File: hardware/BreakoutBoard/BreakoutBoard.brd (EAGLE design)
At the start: 90 x 56 mm, 67 parts, among them J1 CON-71741-2184-TOP, J2 CON-71741-2184-BOT, J3 CON-2X11-RASTER, J4 CON-2X10-RASTER, J5 CON-2X10-RASTER, J6 CON-2X11-RASTER, J7 CON-HTST-105-04-D-RA, M1 MOUNT-HOLE3.3, M2 MOUNT-HOLE3.3, M3 MOUNT-HOLE3.3, M4 MOUNT-HOLE3.3, M5 FIDUCIAL1X2, M6 FIDUCIAL1X2, M7 FIDUCIAL1X2, M8 FIDUCIAL1X2

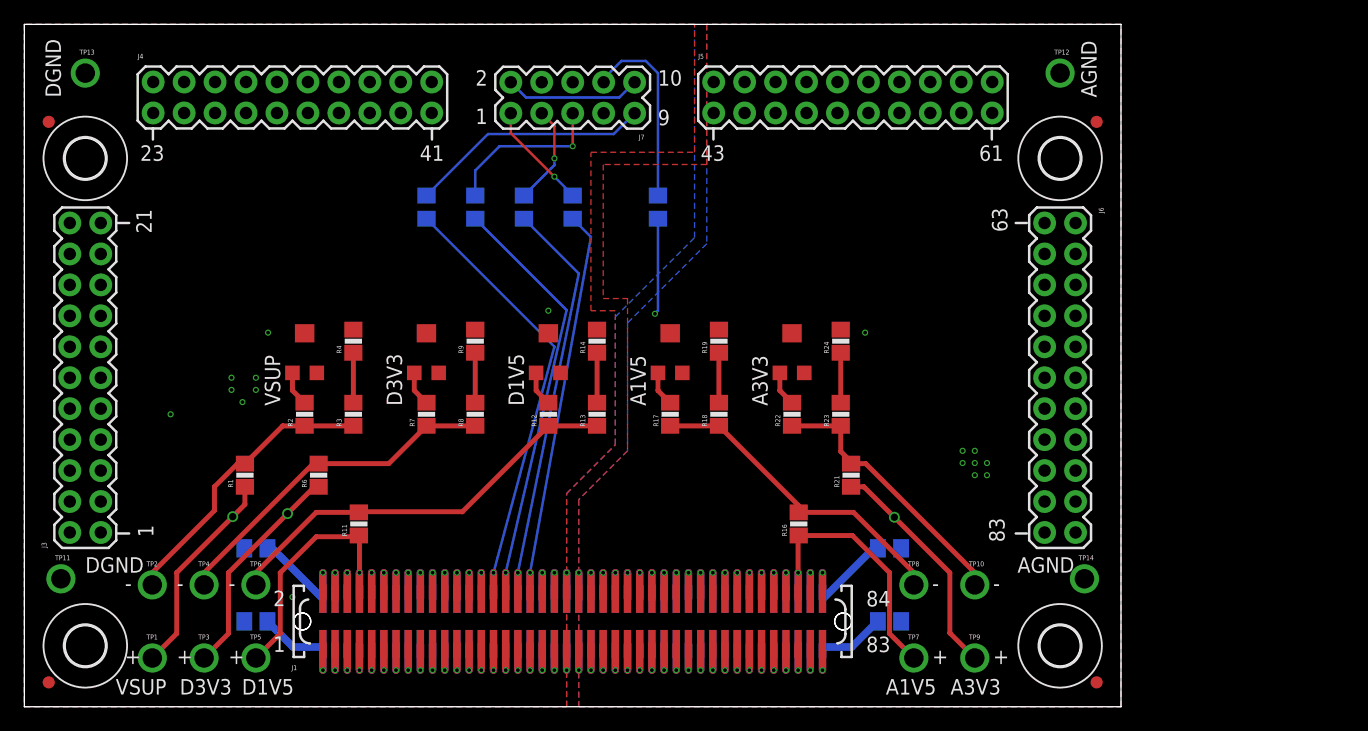
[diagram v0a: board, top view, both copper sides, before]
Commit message: - New connectors added and routed
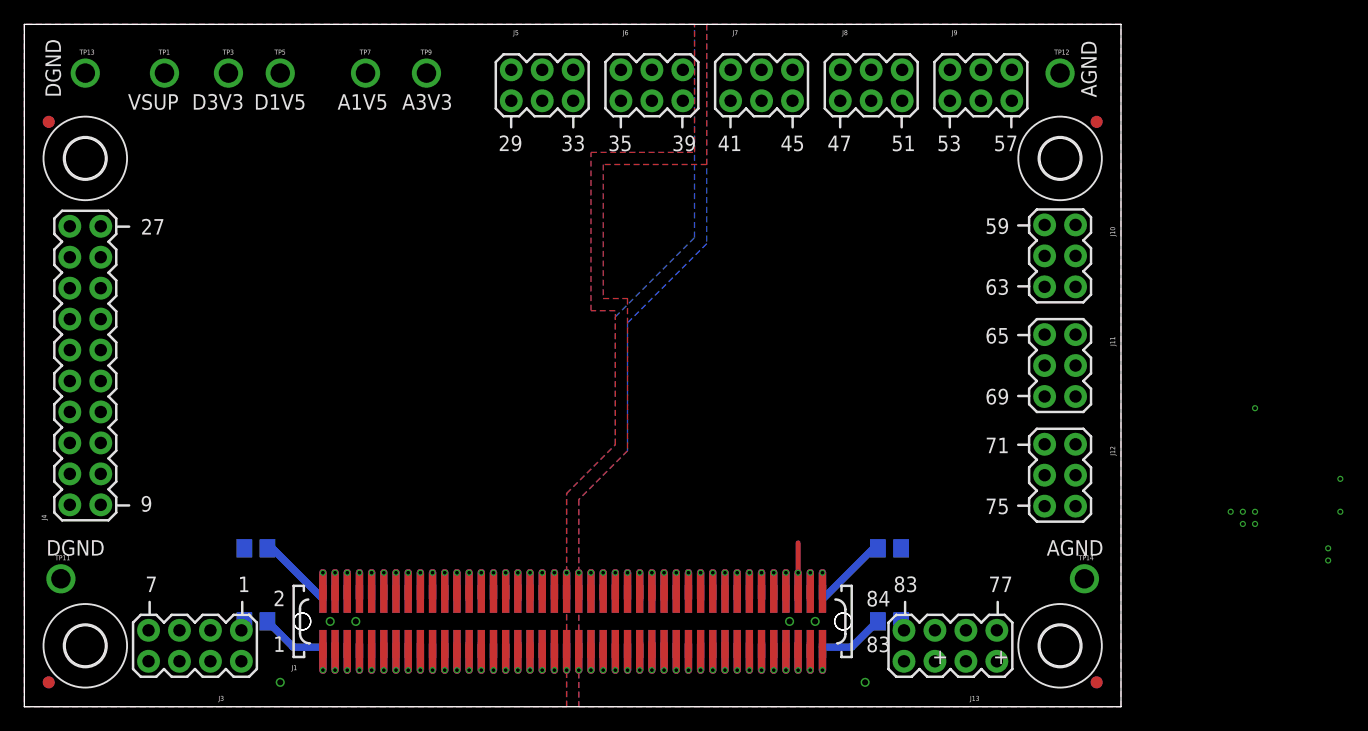
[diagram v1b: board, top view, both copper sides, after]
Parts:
- removed R1, R11, R14, R16, R19, R21, R24, R4, R6, R9: 10, BreakoutBoard:R0805
- removed R10, R15, R20, R25, R5: 1000, BreakoutBoard:TRIMMER-3MM
- removed R12, R13, R17, R18, R2, R22, R23, R26, R27, R28, R29, R3, R30, R7, R8: 0, BreakoutBoard:R0805
- removed TP10, TP8: TESTPOINT-GREEN, BreakoutBoard:TESTPOINT
- removed TP2, TP4, TP6: TESTPOINT-BLUE, BreakoutBoard:TESTPOINT
- added J10, J11, J12, J8, J9: CON-2X3-RASTER, BreakoutBoard:2X6
- added J13: CON-2X4-RASTER, BreakoutBoard:2X8
- J3: value CON-2X11-RASTER -> CON-2X4-RASTER; device BreakoutBoard:2X22 -> BreakoutBoard:2X8
- J5: value CON-2X10-RASTER -> CON-2X3-RASTER; device BreakoutBoard:2X20 -> BreakoutBoard:2X6
- J6: value CON-2X11-RASTER -> CON-2X3-RASTER; device BreakoutBoard:2X22 -> BreakoutBoard:2X6
- J7: value CON-HTST-105-04-D-RA -> CON-2X3-RASTER; device BreakoutBoard:HTST-105-04-D-RA -> BreakoutBoard:2X6
- moved TP7 65.8 mm to (28.0, 52.0)
- moved TP9 65.8 mm to (33.0, 52.0)
- moved TP3 48.0 mm to (16.8, 52.0)
- moved TP5 48.0 mm to (21.0, 52.0)
- moved TP1 48.0 mm to (11.5, 52.0)
- moved J6 41.2 mm to (51.5, 51.0), turned to 0 degrees
- moved J4 27.8 mm to (5.00, 28.0), turned to 90 degrees
- moved LOGO3 27.0 mm to (27.0, 17.0)
- moved J5 25.5 mm to (42.5, 51.0)
- moved J3 23.8 mm to (14.0, 5.00), turned to 180 degrees
- moved LOGO1 21.1 mm to (53.0, 32.0)
- moved LOGO4 20.2 mm to (53.0, 17.0)
- moved J7 15.5 mm to (60.5, 51.0), turned to 0 degrees
- moved LOGO2 11.2 mm to (27.0, 32.0)
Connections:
- removed net A1V5-: R16.2, R17.1, R18.1, TP8.1
- removed net A3V3-: R21.2, R22.1, R23.1, TP10.1
- removed net D1V5-: R11.2, R12.1, R13.1, TP6.1
- removed net D3V3-: R6.2, R7.1, R8.1, TP4.1
- removed net N$10: R17.2, R20.1
- removed net N$11: R22.2, R25.1
- removed net N$13: R2.2, R5.1
- removed net N$14: R3.2, R4.1
- removed net N$15: R13.2, R14.1
- removed net N$16: R23.2, R24.1
- removed net N$4: R10.1, R7.2
- removed net N$5: R8.2, R9.1
- removed net N$8: R12.2, R15.1
- removed net N$9: R18.2, R19.1
- removed net NC: J7.4
- removed net TCK: J7.1, R26.2
- removed net TDI: J7.9, R29.2
- removed net TDO: J7.3, R27.2
- removed net TMS: J7.5, R28.2
- removed net TRST: J7.8, R30.1
- removed net VJTAG: J7.6
- removed net VPUMP: J7.7
- removed net VSUP-: R1.2, R2.1, R3.1, TP2.1
- net 10: now also J4.2; no longer J3.10
- net 11: now also J4.3; no longer J3.11
- net 12: now also J4.4; no longer J3.12
- net 13: now also J4.5; no longer J3.13
- net 14: now also J4.6; no longer J3.14
- net 15: now also J4.7; no longer J3.15
- net 16: now also J4.8; no longer J3.16
- net 17: now also J4.9; no longer J3.17
- net 18: now also J4.10; no longer J3.18
- net 19: now also J4.11; no longer J3.19
- net 20: now also J4.12; no longer J3.20
- net 21: now also J4.13; no longer J3.21
- net 22: now also J4.14; no longer J3.22
- net 23: now also J4.15; no longer J4.1
- net 24: now also J4.16; no longer J4.2
- net 25: now also J4.17; no longer J4.3
- net 26: now also J4.18; no longer J4.4
- net 27: now also J4.19; no longer J4.5
- net 28: now also J4.20; no longer J4.6
- net 29: now also J5.1; no longer J4.7
- net 30: now also J5.2; no longer J4.8, R29.1
- net 31: now also J5.3; no longer J4.9
- net 32: now also J5.4; no longer J4.10, R28.1
- net 33: now also J5.5; no longer J4.11
- net 34: now also J5.6; no longer J4.12, R27.1
- net 35: now also J6.1; no longer J4.13
- net 36: now also J6.2; no longer J4.14, R26.1
- net 37: now also J6.3; no longer J4.15
- net 38: now also J6.4; no longer J4.16, R30.2
- net 39: now also J6.5; no longer J4.17
- net 4: no longer R1.1
- net 40: now also J6.6; no longer J4.18
- net 41: now also J7.1; no longer J4.19
- net 42: now also J7.2; no longer J4.20
- net 43: now also J7.3; no longer J5.1
- net 44: now also J7.4; no longer J5.2
- net 45: now also J7.5; no longer J5.3
- net 46: now also J7.6; no longer J5.4
- net 47: now also J8.1; no longer J5.5
- net 48: now also J8.2; no longer J5.6
- net 49: now also J8.3; no longer J5.7
- net 50: now also J8.4; no longer J5.8
- net 51: now also J8.5; no longer J5.9
- net 52: now also J8.6; no longer J5.10
- net 53: now also J9.1; no longer J5.11
- net 54: now also J9.2; no longer J5.12
- net 55: now also J9.3; no longer J5.13
- net 56: now also J9.4; no longer J5.14
- net 57: now also J9.5; no longer J5.15
- net 58: now also J9.6; no longer J5.16
- net 59: now also J10.1; no longer J5.17
- net 6: no longer R6.1
- net 60: now also J10.2; no longer J5.18
- net 61: now also J10.3; no longer J5.19
- net 62: now also J10.4; no longer J5.20
- net 63: now also J10.5; no longer J6.1
- net 64: now also J10.6; no longer J6.2
- net 65: now also J11.1; no longer J6.3
- net 66: now also J11.2; no longer J6.4
- net 67: now also J11.3; no longer J6.5
- net 68: now also J11.4; no longer J6.6
- net 69: now also J11.5; no longer J6.7
- net 70: now also J11.6; no longer J6.8
- net 71: now also J12.1; no longer J6.9
- net 72: now also J12.2; no longer J6.10
- net 73: now also J12.3; no longer J6.11
- net 74: now also J12.4; no longer J6.12
- net 75: now also J12.5; no longer J6.13
- net 76: now also J12.6; no longer J6.14
- net 77: now also J13.1; no longer J6.15
- net 78: now also J13.2; no longer J6.16
- net 79: now also J13.3; no longer J6.17
- net 8: no longer R11.1
- net 80: now also J13.4; no longer J6.18, R16.1
- net 81: now also J13.5; no longer J6.19
- net 82: now also J13.6; no longer J6.20, R21.1
- net 83: now also J13.7; no longer J6.21
- net 84: now also J13.8; no longer J6.22
- net 9: now also J4.1; no longer J3.9
- net AGND: no longer R19.2, R20.2, R24.2, R25.2
- net DGND: no longer J7.10, J7.2, R10.2, R14.2, R15.2, R4.2, R5.2, R9.2
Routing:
- net 30: track 87.0 -> 46.2 mm
- net 32: track 85.1 -> 46.8 mm
- net 34: track 83.1 -> 47.5 mm
- net D1V5-: track 34.0 -> 0.00 mm
- net 36: track 81.2 -> 48.7 mm
- net D3V3-: track 28.2 -> 0.00 mm
- net A1V5-: track 26.3 -> 0.00 mm
- net 82: track 47.2 -> 21.4 mm, vias 2 -> 1
- net 4: track 45.7 -> 21.4 mm, vias 2 -> 1
- net VSUP-: track 23.7 -> 0.00 mm
- net 6: track 48.7 -> 25.5 mm, vias 2 -> 1
- net A3V3-: track 22.4 -> 0.00 mm
- net 8: track 51.2 -> 29.6 mm
- net 80: track 49.4 -> 28.0 mm
- net TDI: track 19.9 -> 0.00 mm
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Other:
- board text added: "27"
- board text added: "29"
- board text added: "33"
- board text added: "35"
- board text added: "39"
- board text added: "45"
- board text added: "47"
- board text added: "51"
- board text added: "53"
- board text added: "57"
- board text added: "59"
- board text added: "65"
- board text added: "69"
- board text added: "7"
- board text added: "71"
- board text added: "75"
- board text added: "77"
- board text added: "9"
- board text removed: "-"
- board text removed: "21"
- board text removed: "23"
- board text removed: "43"
- board text removed: "61"

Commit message: - wires moved to different layer - docu layer - Supply voltages
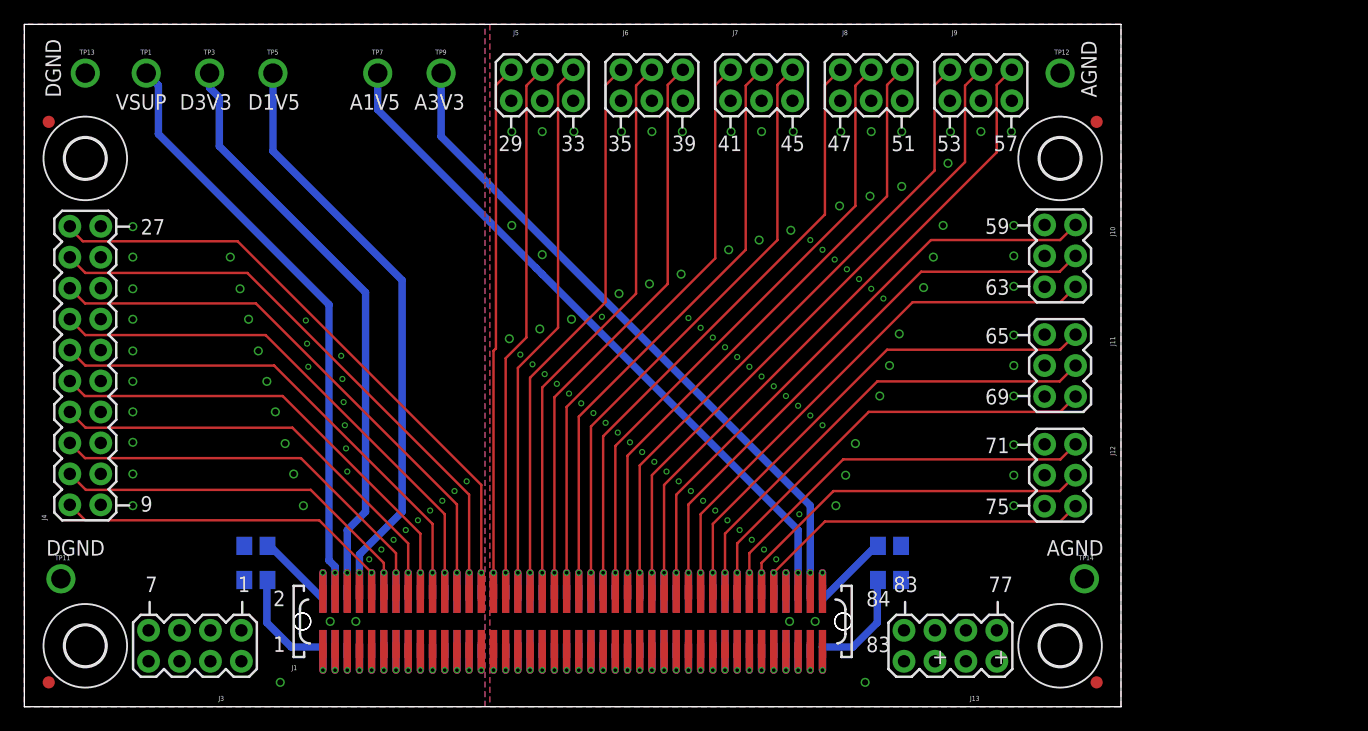
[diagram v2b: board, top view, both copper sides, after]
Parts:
- moved LOGO3 42.7 mm to (39.0, 58.0)
- moved LOGO4 41.1 mm to (50.0, 58.0)
- moved LOGO1 36.1 mm to (28.0, 58.0)
- moved LOGO2 27.9 mm to (17.0, 58.0)
- moved R31 3.40 mm to (19.0, 10.4)
- moved R33 3.40 mm to (71.0, 10.4)
- moved TP3 1.55 mm to (15.2, 52.0)
- moved TP1 1.50 mm to (10.0, 52.0)
- moved TP9 1.20 mm to (34.2, 52.0)
- moved TP7 1.00 mm to (29.0, 52.0)
- moved TP5 0.60 mm to (20.4, 52.0)
- moved R32 0.20 mm to (19.0, 13.2)
- moved R34 0.20 mm to (71.0, 13.2)
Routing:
- net 82: track 21.4 -> 75.0 mm
- net 80: track 28.0 -> 80.8 mm
- net 4: track 21.4 -> 68.9 mm
- net 6: track 25.5 -> 72.4 mm
- net 8: track 29.6 -> 76.5 mm
- net 83: track 17.7 -> 21.2 mm
- net 1: track 17.6 -> 20.5 mm
